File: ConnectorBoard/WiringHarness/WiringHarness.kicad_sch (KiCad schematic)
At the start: 23 parts, among them J1 Barrel_Jack, J2 Conn_01x03, J3 Conn_01x03, J4 Conn_02x05_Odd_Even, J5 Socket, J6 Qwiic, J7 Header, U1 L7805, U2 TLV75533PDBV

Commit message: Not sure what changes, but it was minor...
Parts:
- J5: Digikey S7039-ND -> S7037-ND; Vendor S7039-ND -> S7037-ND
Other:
- note added: "Additional GPIO for sensors in the maze."
- moved on the sheet: J5
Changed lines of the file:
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@@
 (kicad_sch (version 20230121) (generator eeschema)
   (paper "A4")
-  (junction (at 74.93 113.03) (diameter 0) (color 0 0 0 0)
+  (junction (at 148.59 110.49) (diameter 0) (color 0 0 0 0)
   )
   (junction (at 74.93 90.17) (diameter 0) (color 0 0 0 0)
@@
   (junction (at 93.98 80.01) (diameter 0) (color 0 0 0 0)
   )
+  (junction (at 74.93 120.65) (diameter 0) (color 0 0 0 0)
+  )
   (junction (at 184.15 91.44) (diameter 0) (color 0 0 0 0)
   )
@@
   )
   (junction (at 82.55 90.17) (diameter 0) (color 0 0 0 0)
-  )
-  (junction (at 148.59 110.49) (diameter 0) (color 0 0 0 0)
   )
   (junction (at 199.39 91.44) (diameter 0) (color 0 0 0 0)
@@
     (stroke (width 0) (type default))
   )
-  (wire (pts (xy 148.59 111.76) (xy 119.38 111.76))
+  (wire (pts (xy 119.38 119.38) (xy 148.59 119.38))
     (stroke (width 0) (type default))
   )
@@
     (stroke (width 0) (type default))
   )
+  (wire (pts (xy 127 123.19) (xy 127 116.84))
+    (stroke (width 0) (type default))
+  )
   (wire (pts (xy 199.39 91.44) (xy 194.31 91.44))
     (stroke (width 0) (type default))
@@
     (stroke (width 0) (type default))
   )
-  (wire (pts (xy 74.93 113.03) (xy 121.92 113.03))
-    (stroke (width 0) (type default))
-  )
-  (wire (pts (xy 74.93 113.03) (xy 74.93 116.84))
+  (wire (pts (xy 74.93 120.65) (xy 121.92 120.65))
     (stroke (width 0) (type default))
   )
@@
     (stroke (width 0) (type default))
   )
-  (wire (pts (xy 124.46 109.22) (xy 124.46 116.84))
+  (wire (pts (xy 124.46 109.22) (xy 124.46 123.19))
     (stroke (width 0) (type default))
   )
@@
     (stroke (width 0) (type default))
   )
+  (wire (pts (xy 74.93 120.65) (xy 74.93 124.46))
+    (stroke (width 0) (type default))
+  )
   (wire (pts (xy 91.44 99.06) (xy 99.06 99.06))
     (stroke (width 0) (type default))
@@
     (stroke (width 0) (type default))
   )
-  (wire (pts (xy 148.59 110.49) (xy 148.59 111.76))
-    (stroke (width 0) (type default))
-  )
   (wire (pts (xy 74.93 90.17) (xy 82.55 90.17))
     (stroke (width 0) (type default))
   )
+  (wire (pts (xy 148.59 110.49) (xy 148.59 119.38))
+    (stroke (width 0) (type default))
+  )
   (wire (pts (xy 168.91 91.44) (xy 168.91 93.98))
     (stroke (width 0) (type default))
@@
     (stroke (width 0) (type default))
   )
-  (wire (pts (xy 74.93 90.17) (xy 74.93 113.03))
+  (wire (pts (xy 74.93 90.17) (xy 74.93 120.65))
     (stroke (width 0) (type default))
   )
@@
     (stroke (width 0) (type default))
   )
-  (wire (pts (xy 121.92 113.03) (xy 121.92 116.84))
+  (wire (pts (xy 121.92 120.65) (xy 121.92 123.19))
     (stroke (width 0) (type default))
   )
@@
     (stroke (width 0) (type default))
   )
-  (wire (pts (xy 119.38 111.76) (xy 119.38 116.84))
+  (wire (pts (xy 119.38 119.38) (xy 119.38 123.19))
     (stroke (width 0) (type default))
   )
@@
     (stroke (width 0) (type default))
   )
-  (text "Connector for 4 digit display." (at 109.22 132.08 0)
+  (text "Connector for 4 digit display." (at 109.22 139.7 0)
     (effects (font (size 1.27 1.27)) (justify left bottom))
   )
@@
     (effects (font (size 1.27 1.27)) (justify left bottom))
   )
+  (text "Additional GPIO for \nsensors in the maze." (at 81.28 111.76 0)
+    (effects (font (size 1.27 1.27)) (justify left bottom))
+  )
   (label "Vsys" (at 97.79 80.01 0) (fields_autoplaced)
     (effects (font (size 1.27 1.27)) (justify left bottom))
@@
     (effects (font (size 1.27 1.27)) (justify left bottom))
   )
-  (symbol (lib_id "power:GND") (at 74.93 116.84 0) (unit 1)
-    (in_bom yes) (on_board yes) (dnp no) (fields_autoplaced)
-    (property "Reference" "#PWR02" (at 74.93 123.19 0)
-      (effects (font (size 1.27 1.27)) hide)
-    )
-    (property "Value" "GND" (at 74.93 121.92 0)
-      (effects (font (size 1.27 1.27)))
-    )
-    (property "Footprint" "" (at 74.93 116.84 0)
-      (effects (font (size 1.27 1.27)) hide)
-    )
-    (property "Datasheet" "" (at 74.93 116.84 0)
+  (symbol (lib_id "power:GND") (at 74.93 124.46 0) (unit 1)
+    (in_bom yes) (on_board yes) (dnp no) (fields_autoplaced)
+    (property "Reference" "#PWR02" (at 74.93 130.81 0)
+      (effects (font (size 1.27 1.27)) hide)
+    )
+    (property "Value" "GND" (at 74.93 129.54 0)
+      (effects (font (size 1.27 1.27)))
+    )
+    (property "Footprint" "" (at 74.93 124.46 0)
+      (effects (font (size 1.27 1.27)) hide)
+    )
+    (property "Datasheet" "" (at 74.93 124.46 0)
       (effects (font (size 1.27 1.27)) hide)
     )
@@
     )
   )
-  (symbol (lib_id "Connector_Generic:Conn_01x04") (at 124.46 121.92 270) (unit 1)
+  (symbol (lib_id "Connector_Generic:Conn_01x04") (at 124.46 128.27 270) (unit 1)
     (in_bom yes) (on_board yes) (dnp no)
-    (property "Reference" "J5" (at 123.19 125.73 90)
-      (effects (font (size 1.27 1.27)))
-    )
-    (property "Value" "Socket" (at 123.19 128.27 90)
-      (effects (font (size 1.27 1.27)))
-    )
-    (property "Footprint" "Connector_PinSocket_2.54mm:PinSocket_1x04_P2.54mm_Vertical" (at 124.46 121.92 0)
-      (effects (font (size 1.27 1.27)) hide)
-    )
-    (property "Datasheet" "https://mm.digikey.com/Volume0/opasdata/d220001/medias/docus/937/Female_Headers.100_DS.pdf" (at 124.46 121.92 0)
-      (effects (font (size 1.27 1.27)) hide)
-    )
-    (property "Digikey" "S7039-ND" (at 124.46 121.92 0)
-      (effects (font (size 1.27 1.27)) hide)
-    )
-    (property "Vendor" "S7039-ND" (at 124.46 121.92 0)
-      (effects (font (size 1.27 1.27)) hide)
-    )
+    (property "Reference" "J5" (at 123.19 132.08 90)
+      (effects (font (size 1.27 1.27)))
+    )
+    (property "Value" "Socket" (at 123.19 134.62 90)
+      (effects (font (size 1.27 1.27)))
+    )
+    (property "Footprint" "Connector_PinSocket_2.54mm:PinSocket_1x04_P2.54mm_Vertical" (at 124.46 128.27 0)
+      (effects (font (size 1.27 1.27)) hide)
+    )
+    (property "Datasheet" "https://mm.digikey.com/Volume0/opasdata/d220001/medias/docus/937/Female_Headers.100_DS.pdf" (at 124.46 128.27 0)
+      (effects (font (size 1.27 1.27)) hide)
+    )
+    (property "Digikey" "S7037-ND" (at 124.46 128.27 0)
+      (effects (font (size 1.27 1.27)) hide)
+    )
+    (property "Vendor" "S7037-ND" (at 124.46 128.27 0)
+      (effects (font (size 1.27 1.27)) hide)
+    )

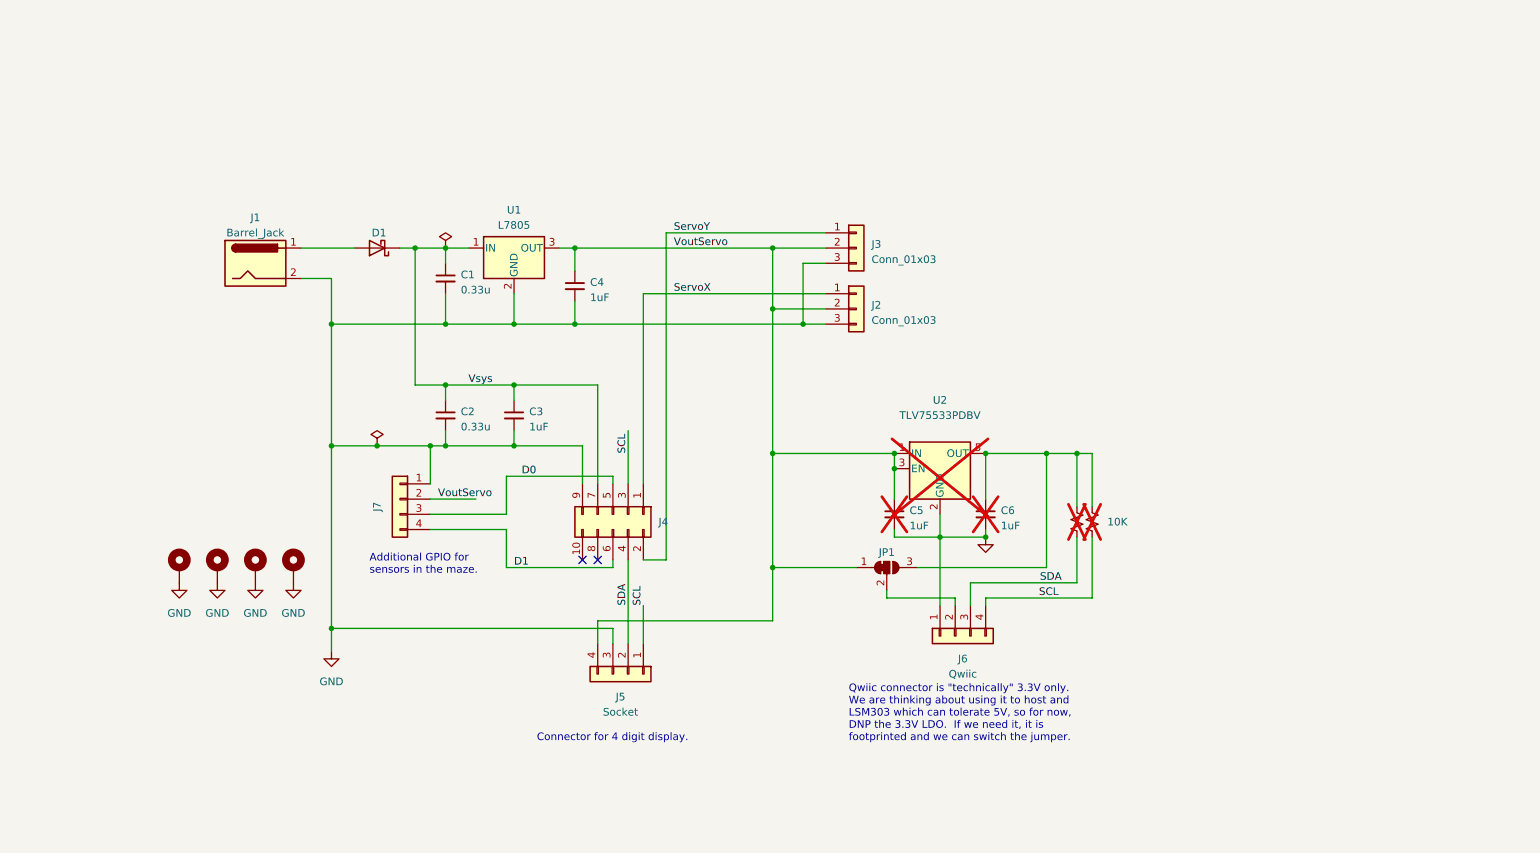
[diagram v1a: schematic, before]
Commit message: variable servo source
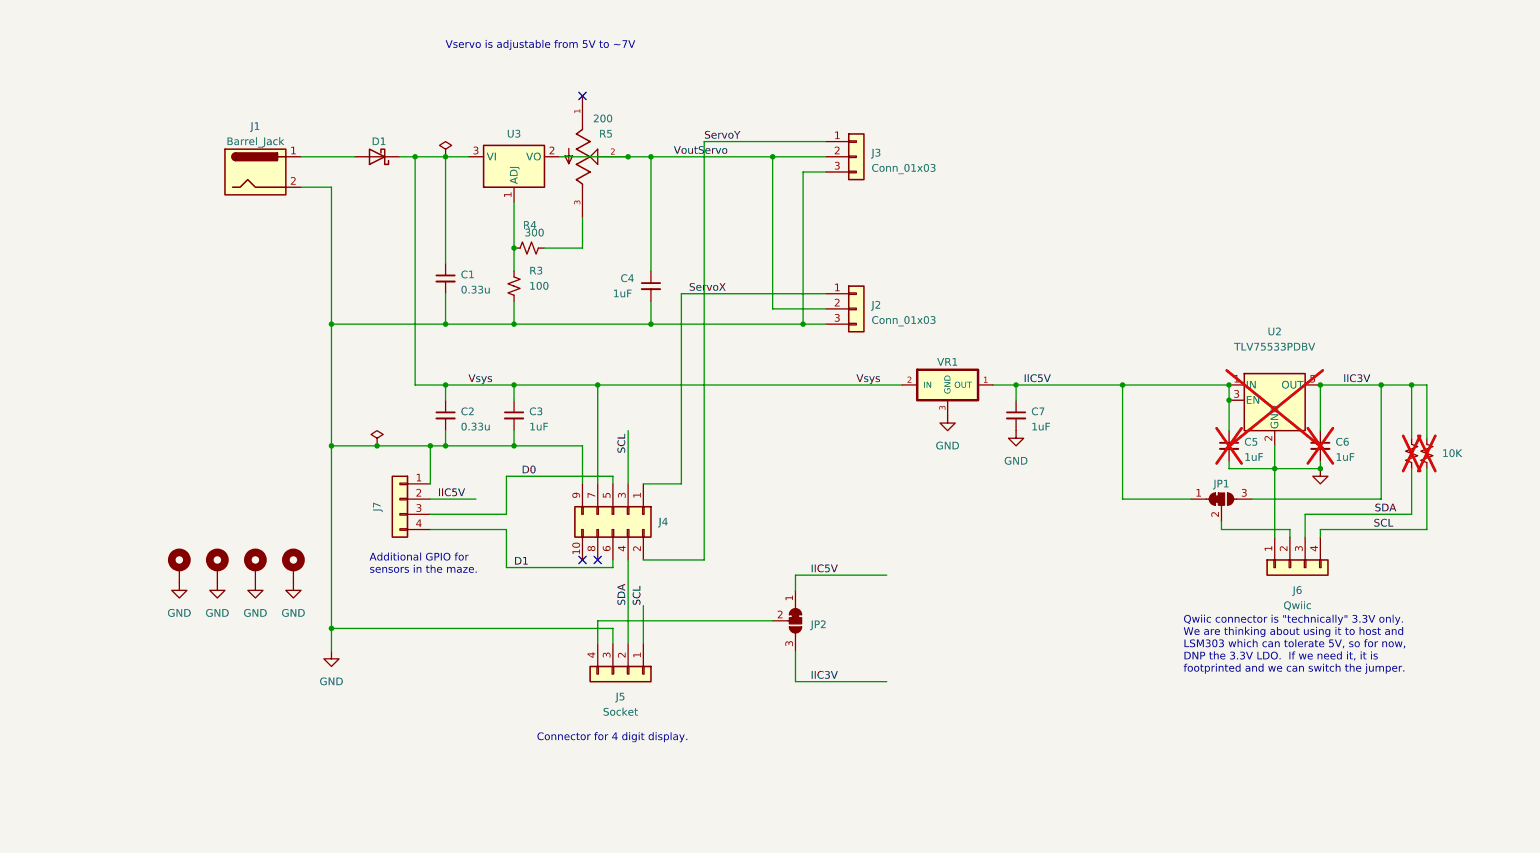
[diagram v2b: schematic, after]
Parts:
- removed U1: L7805, Package_TO_SOT_SMD:TO-252-2, symbol Regulator_Linear:L7805
- added C7: 1uF, Capacitor_SMD:C_0603_1608Metric, symbol Device:C_Small
- added JP2: SolderJumper_3_Bridged12, Jumper:SolderJumper-3_P1.3mm_Bridged12_RoundedPad1.0x1.5mm, symbol Jumper:SolderJumper_3_Bridged12
- added R3: 100, Resistor_SMD:R_0603_1608Metric, symbol Device:R_Small_US
- added R4: 300, Resistor_SMD:R_0603_1608Metric, symbol Device:R_Small_US
- added R5: 200, Passives:TRIM_TC33X-2-201E, symbol StockedComponents:TC33X-2-201E
- added U3: NCP1117-ADJ_SOT223, Package_TO_SOT_SMD:SOT-223-3_TabPin2, symbol Regulator_Linear:NCP1117-ADJ_SOT223
- added VR1: TLV76050DBZR, TexasInstruments:SOT95P237X112-3N, symbol StockedComponents:TLV76050DBZR
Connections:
- net GND: now also C7.2, R3.2, VR1.3 (GND)
- net VoutServo: now also R5.2, U3.2 (VO); no longer C5.1, J5.4 (Pin_4), J7.2 (Pin_2), JP1.1 (A), U2.1 (IN), U2.3 (EN)
- net Vsys: now also U3.3 (VI), VR1.2 (IN)
- net IIC3V: now reaches C6.1, JP1.3 (B), R1.1, R2.1, U2.5 (OUT)
- net IIC3V: now also JP2.3 (B)
- new net: J5.4 (Pin_4), JP2.2 (C)
- new net: R3.1, R4.1, U3.1 (ADJ)
- new net: R4.2, R5.3
- new net IIC5V: C5.1, C7.1, J7.2 (Pin_2), JP1.1 (A), JP2.1 (A), U2.1 (IN), U2.3 (EN), VR1.1 (OUT)
- no-connect marks 2 -> 3
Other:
- note added: "Vservo is adjustable from 5V to ~7V"
- moved on the sheet: C4, C5, C6, D1, J1, J3, J6, JP1, U2

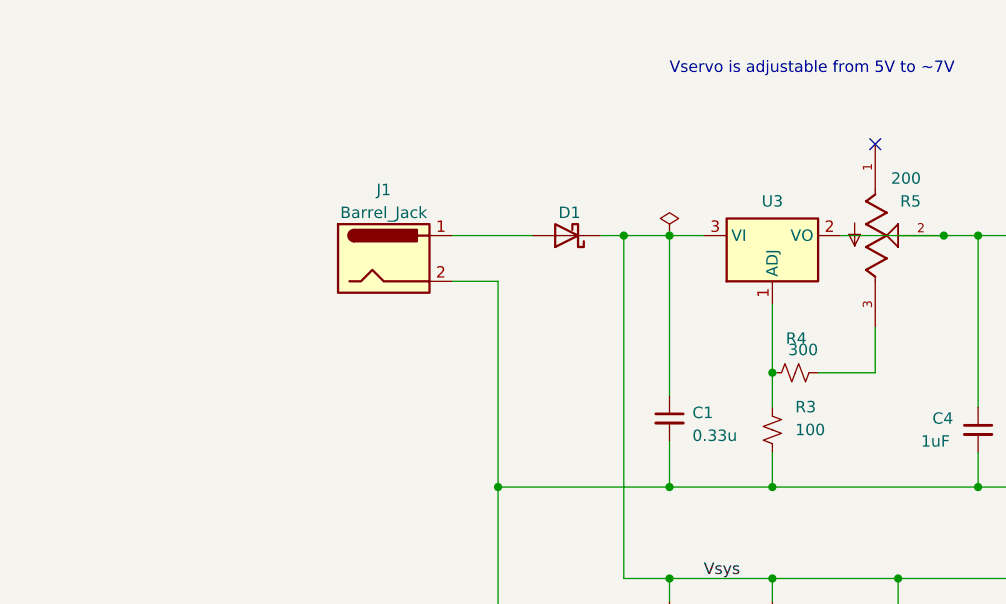
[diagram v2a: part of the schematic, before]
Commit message: initial rework and controller bom
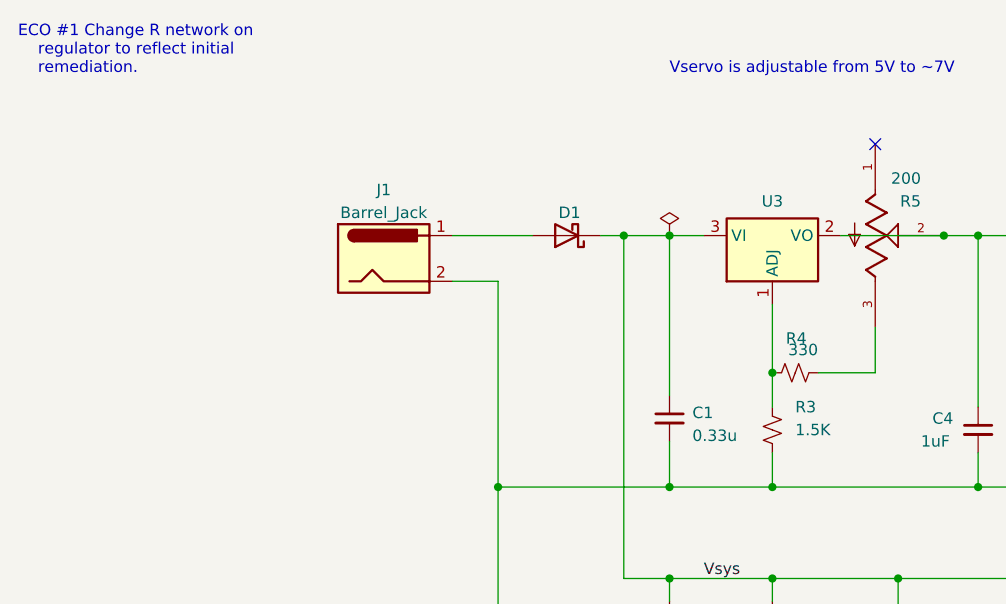
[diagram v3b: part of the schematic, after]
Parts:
- R3: value 100 -> 1.5K
- R4: value 300 -> 330
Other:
- note added: "ECO #1 Change R network on regulator to reflect initial remediation."
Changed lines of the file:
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@@
+    (effects (font (size 1.27 1.27)) (justify left bottom))
+  )
+  (text "ECO #1 Change R network on \n	regulator to reflect initial \n	remediation."
+    (at 21.59 24.13 0)
     (effects (font (size 1.27 1.27)) (justify left bottom))
   )
@@
       (effects (font (size 1.27 1.27)) (justify left))
     )
-    (property "Value" "100" (at 107.95 63.5 0)
+    (property "Value" "1.5K" (at 107.95 63.5 0)
       (effects (font (size 1.27 1.27)) (justify left))
     )
@@
       (effects (font (size 1.27 1.27)) (justify left))
     )
-    (property "Value" "300" (at 110.49 54.61 90)
+    (property "Value" "330" (at 110.49 54.61 90)
       (effects (font (size 1.27 1.27)) (justify left))
     )

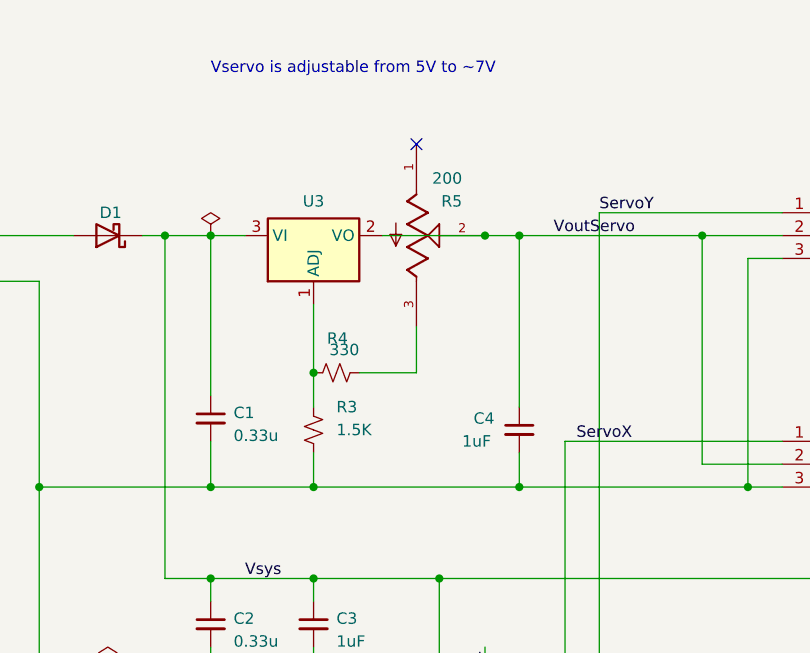
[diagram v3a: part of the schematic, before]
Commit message: Fix the bias network on the regulator.
Close #6
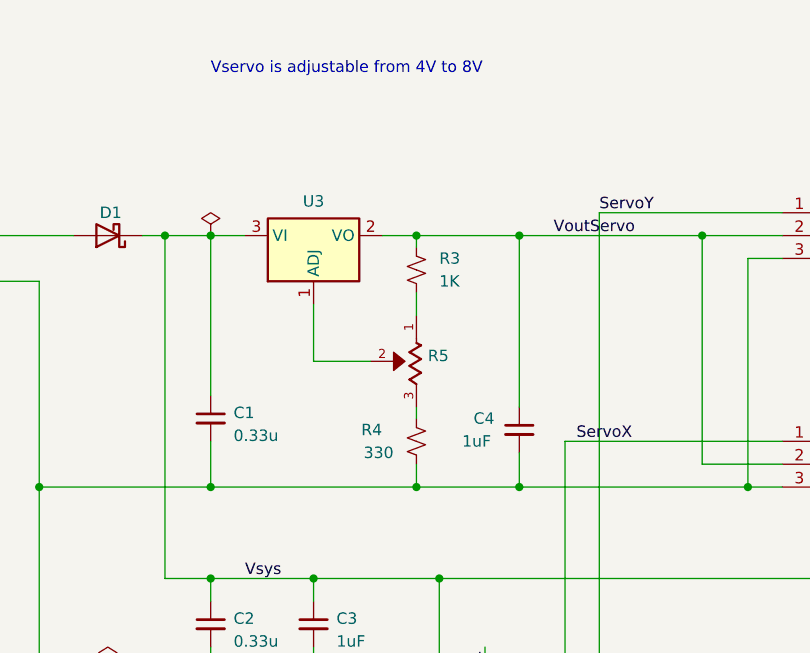
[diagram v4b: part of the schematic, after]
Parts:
- R3: value 1.5K -> 1K
- R5: value 200 -> TC33X-2-201E; AVAILABILITY (none) -> Unavailable; DigiKey TC33X-2-201ECT-ND -> (none); Digikey TC33X-2-201ECT-ND -> (none); Vendor TC33X-2-201ECT-ND -> (none)
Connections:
- net GND: now also R4.1; no longer R3.2
- net VoutServo: now also R3.1; no longer R5.2
- net at R5.1: now also R3.2
- new net: R5.2, U3.1 (ADJ)
- no-connect marks 3 -> 2
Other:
- note added: "Vservo is adjustable from 4V to 8V"
- note removed: "Vservo is adjustable from 5V to ~7V"
- moved on the sheet: R3, R4
